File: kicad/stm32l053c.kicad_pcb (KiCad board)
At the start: 2 copper layers, 52 x 35 mm, 40 parts, among them P1 SWD, P2 PWR, Q1 BC807, SW1 SW_PUSH, SW2 SW_PUSH, SW3 SW_PUSH, U1 STM32L053C8_LQFP48, U2 TLV61225, U3 um66t, Y1 Crystal

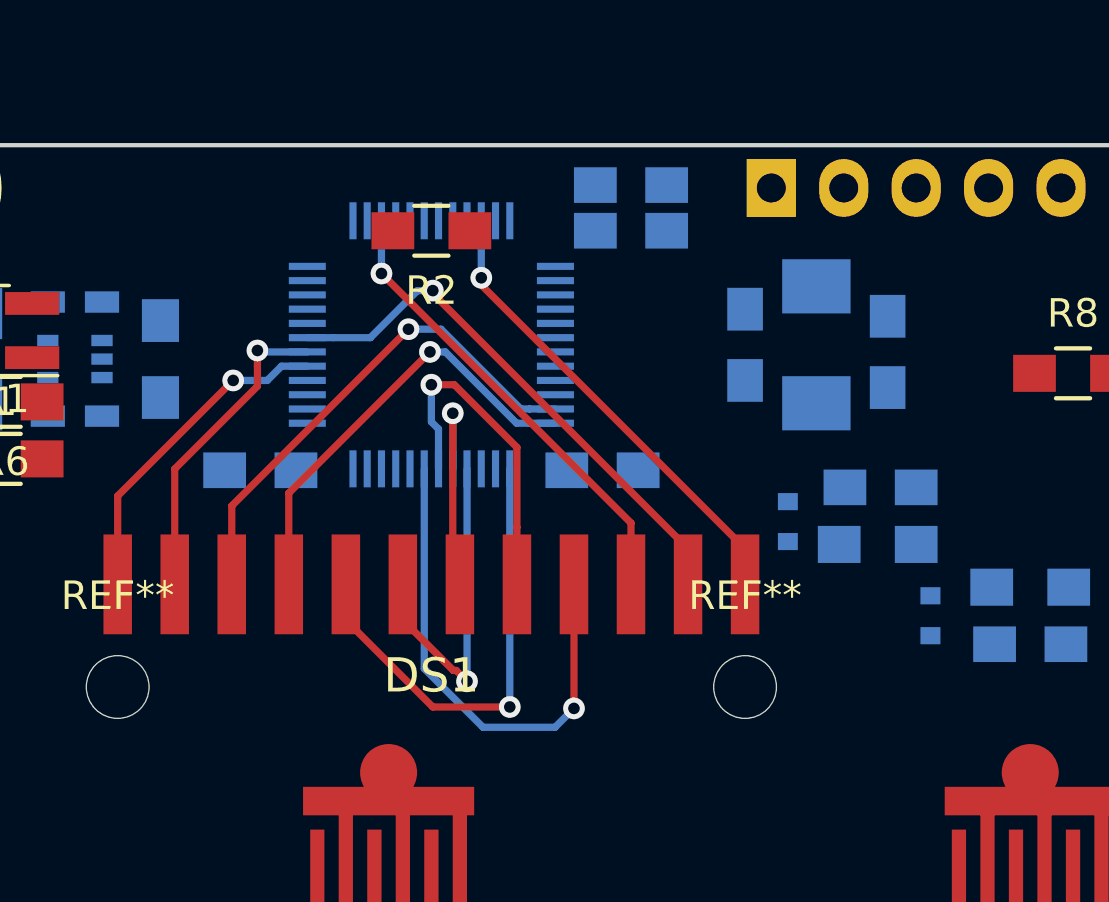
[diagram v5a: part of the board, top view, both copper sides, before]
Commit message: Re-wired the zebra strip
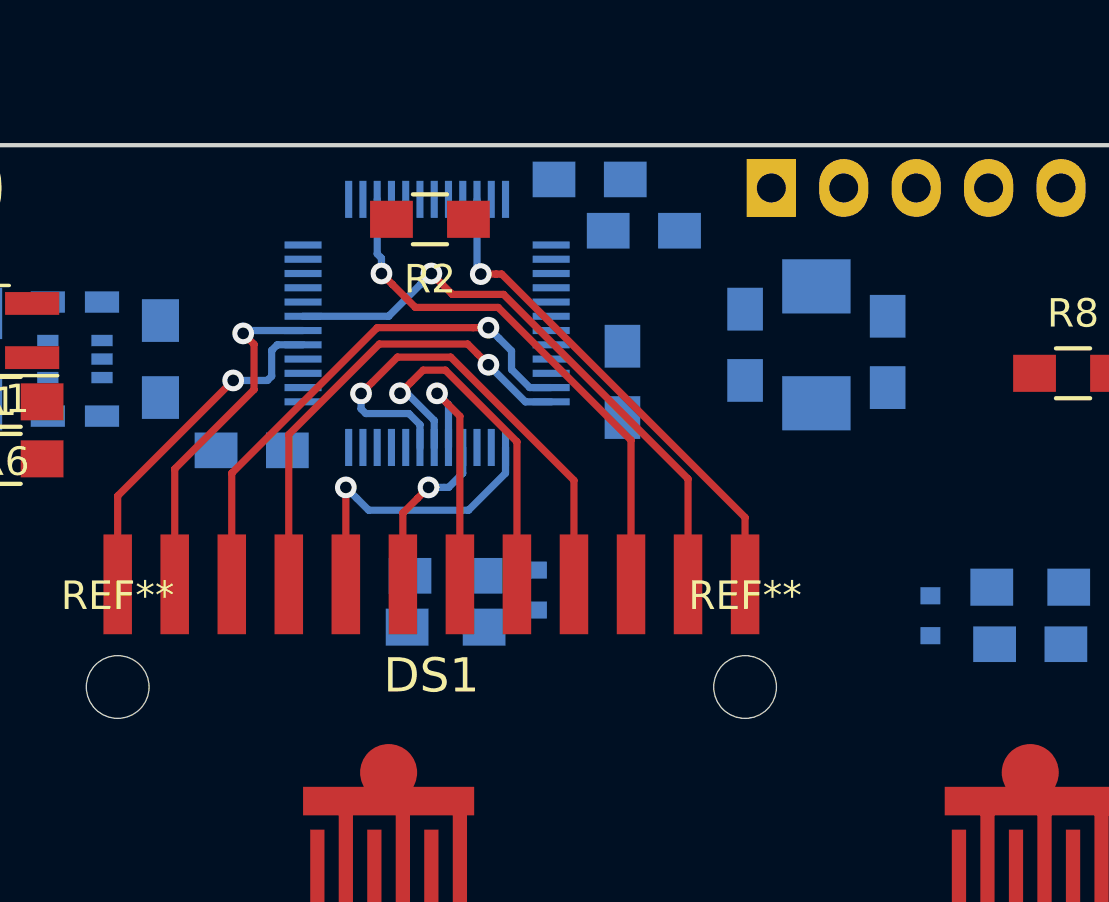
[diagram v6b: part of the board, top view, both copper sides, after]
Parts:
- moved C10 15.6 mm to (143.5, 100.7), turned to 180 degrees
- moved R4 15.4 mm to (143.5, 102.5), turned to 180 degrees
- moved C1 10.2 mm to (148.6, 86.8)
- moved D2 9.12 mm to (146.7, 101.2)
- moved C3 6.91 mm to (149.7, 93.9), turned to 90 degrees
- moved U1 0.76 mm to (142.8, 91.8)
- moved C2 0.76 mm to (136.7, 96.3)
- moved C4 0.45 mm to (150.4, 88.6)
- moved R2 0.40 mm to (142.9, 88.2)
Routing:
- net /LCD_SEG2: track 16.6 -> 12.0 mm
- net /LCD_SEG3: track 11.8 -> 7.33 mm
- net /LCD_SEG7: track 16.4 -> 18.9 mm
- net /LCD_COM2: track 19.1 -> 20.8 mm
- net /LCD_SEG5: track 11.8 -> 13.0 mm
- net /LCD_COM3: track 16.6 -> 17.8 mm
- net /LCD_COM1: track 11.2 -> 12.3 mm
- net /LCD_SEG4: track 8.05 -> 9.10 mm
- net /LCD_SEG1: track 15.6 -> 16.6 mm
- net /LCD_COM0: track 11.6 -> 12.3 mm
- net /LCD_SEG6: track 17.7 -> 17.1 mm
- net /LCD_SEG0: track 17.8 -> 18.5 mm

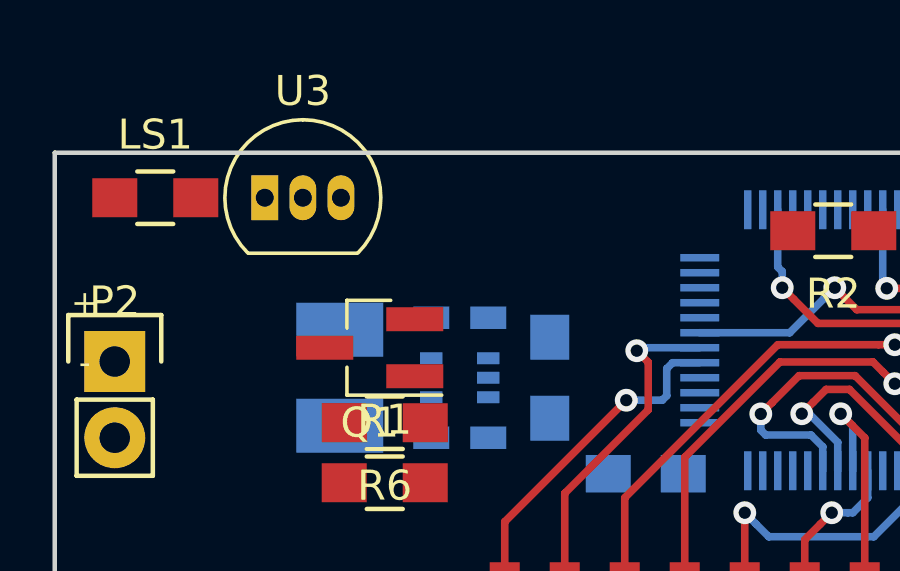
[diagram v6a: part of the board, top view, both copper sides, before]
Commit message: The NPN is needed to completely disconnect the buzzer, otherwise it continually uses power
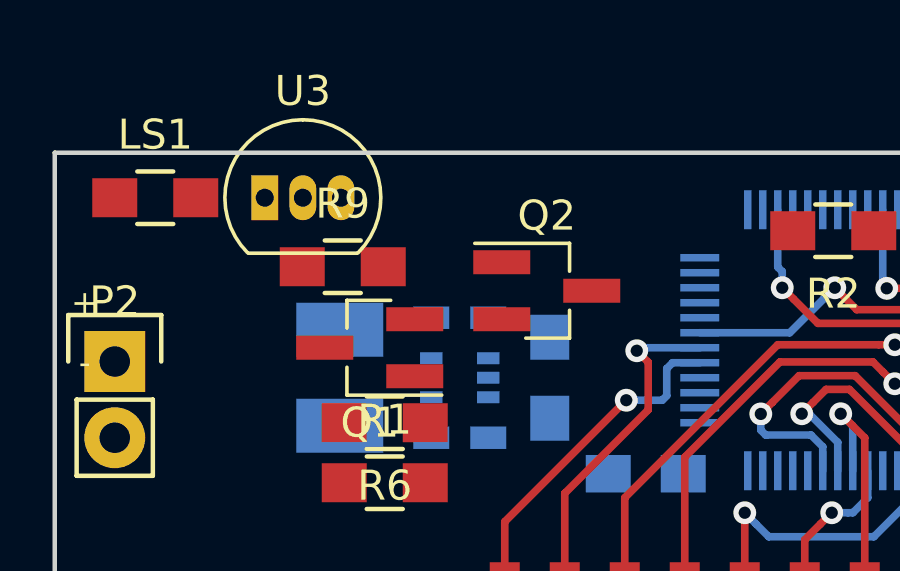
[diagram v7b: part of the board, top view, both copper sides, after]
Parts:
- added Q2: BC817, TO_SOT_Packages_SMD:SOT-23_Handsoldering, F.Cu at (133.4, 90.2)
- added R9: 220, Resistors_SMD:R_0805_HandSoldering, F.Cu at (126.6, 89.4)
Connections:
- Q1 pad 1: Net-(Q1-Pad1) -> /PNP_BASE
- R6 pad 1: Net-(Q1-Pad1) -> Net-(Q2-Pad3)
- R6 pad 2: Net-(R1-Pad1) -> /PNP_BASE

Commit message: Crystal & melody footprints
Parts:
- removed R8: 0, Resistors_SMD:R_0805_HandSoldering
- added R10: 2K2, Resistors_SMD:R_0805_HandSoldering, F.Cu at (127.9, 99.2)
- added SW4: SW_SPDT, Buttons_Switches_SMD:SW_SPST_B3U-1100P, F.Cu at (136.1, 86.9)
- C6, C7: value 20pF -> 4.3pF; footprint Capacitors_SMD:C_0805_HandSoldering -> Capacitors_SMD:C_0603_HandSoldering; moved to F.Cu
- P2: moved to B.Cu
- U3: footprint TO_SOT_Packages_THT:TO-92_Inline_Narrow_Oval -> theapi:UM66T_MELODY; moved to B.Cu
- Y1: value Crystal -> Crystal_GND23; footprint Crystals:ABM3 -> Crystals:Crystal_SMD_SeikoEpson_MC306-4pin_8.0x3.2mm_HandSoldering
- moved R2 5.96 mm to (148.8, 86.8), turned to 0 degrees
- moved C7 4.10 mm to (156.5, 96.1), turned to 0 degrees
- moved C6 2.92 mm to (156.5, 94.1), turned to 0 degrees
- moved U3 2.54 mm to (126.5, 87.1), turned to 180 degrees
- moved Y1 2.50 mm to (156.5, 95.1), turned to 0 degrees
- moved C2 1.77 mm to (137.9, 97.6), turned to 270 degrees
- moved P1 1.50 mm to (155.8, 88.3)
- moved R7 1.43 mm to (133.8, 94.5)
- moved C3 0.76 mm to (150.4, 94.2)
- moved C4 0.58 mm to (150.8, 89.1)
- moved C1 0.56 mm to (148.8, 87.3)
- turned P2 to 180 degrees
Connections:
- C3 pad 1: /VDDA -> VDD
- R9 pad 2: /NPN_BASE -> Net-(R9-Pad2)
- U1 pad 14: Net-(U1-Pad14) -> (no net)
- U1 pad 15: PA5 -> (no net)
- U1 pad 2: Net-(U1-Pad2) -> (no net)
- U1 pad 20: Net-(U1-Pad20) -> (no net)
- U1 pad 21: Net-(U1-Pad21) -> (no net)
- U1 pad 26: Net-(U1-Pad26) -> (no net)
- U1 pad 27: Net-(U1-Pad27) -> (no net)
- U1 pad 28: Net-(U1-Pad28) -> (no net)
- U1 pad 32: Net-(U1-Pad32) -> (no net)
- U1 pad 33: Net-(U1-Pad33) -> (no net)
- U1 pad 38: Net-(U1-Pad38) -> (no net)
- U1 pad 43: Net-(U1-Pad43) -> (no net)
- U1 pad 45: Net-(U1-Pad45) -> (no net)
- U1 pad 5: Net-(U1-Pad5) -> (no net)
- U1 pad 6: Net-(U1-Pad6) -> (no net)
- U1 pad 9: /VDDA -> VDD
- Y1 pad 1: /OSC32_OUT -> /OSC32_IN
- Y1 pad 2: /OSC32_IN -> (no net)
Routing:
- net SWDIO: track 0.00 -> 28.0 mm, vias 0 -> 1
- net SWCLK: track 0.00 -> 22.4 mm, vias 0 -> 1
- net /OSC32_OUT: track 0.00 -> 14.7 mm, vias 0 -> 1
- net Earth: track 0.00 -> 12.5 mm
- net /OSC32_IN: track 0.00 -> 11.3 mm, vias 0 -> 1
- net /WAKEUP_PIN1: track 0.00 -> 8.80 mm
- net VDD: track 0.00 -> 8.72 mm
- net Net-(R2-Pad1): track 0.00 -> 5.23 mm, vias 0 -> 1
- net /VLCD: track 0.00 -> 2.30 mm
- net /LCD_SEG2: track 12.0 -> 10.9 mm
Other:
- board text added: "SWDIO"
- board text removed: "DIO"
